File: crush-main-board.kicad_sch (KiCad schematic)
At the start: 37 parts, among them J1 4x4_Header, J10 3x3 Header, J11 3x3 Header, J12 3x2 Header, J13 3x4_Header, J14 3x4_Header, J15 2157601008, J16 Conn_01x02, J17 Conn_01x02, J2 4x4_Header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

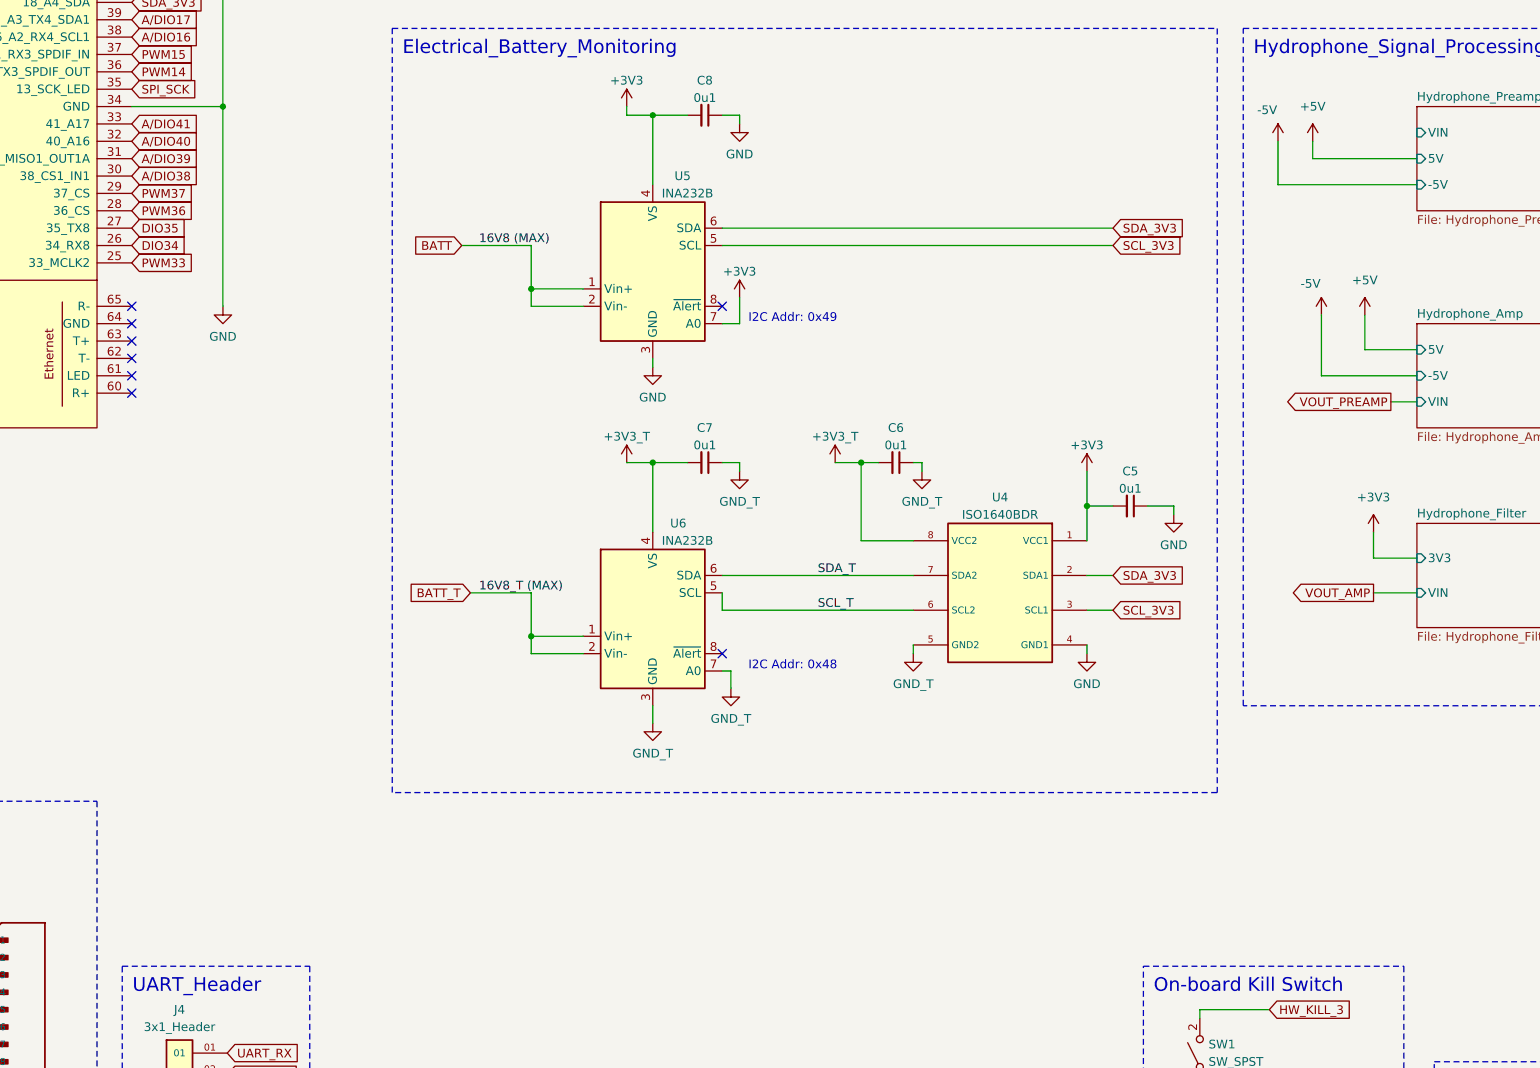
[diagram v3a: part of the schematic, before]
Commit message: Add BNC connection to VIN of hydrophone pre-amp subcircuit
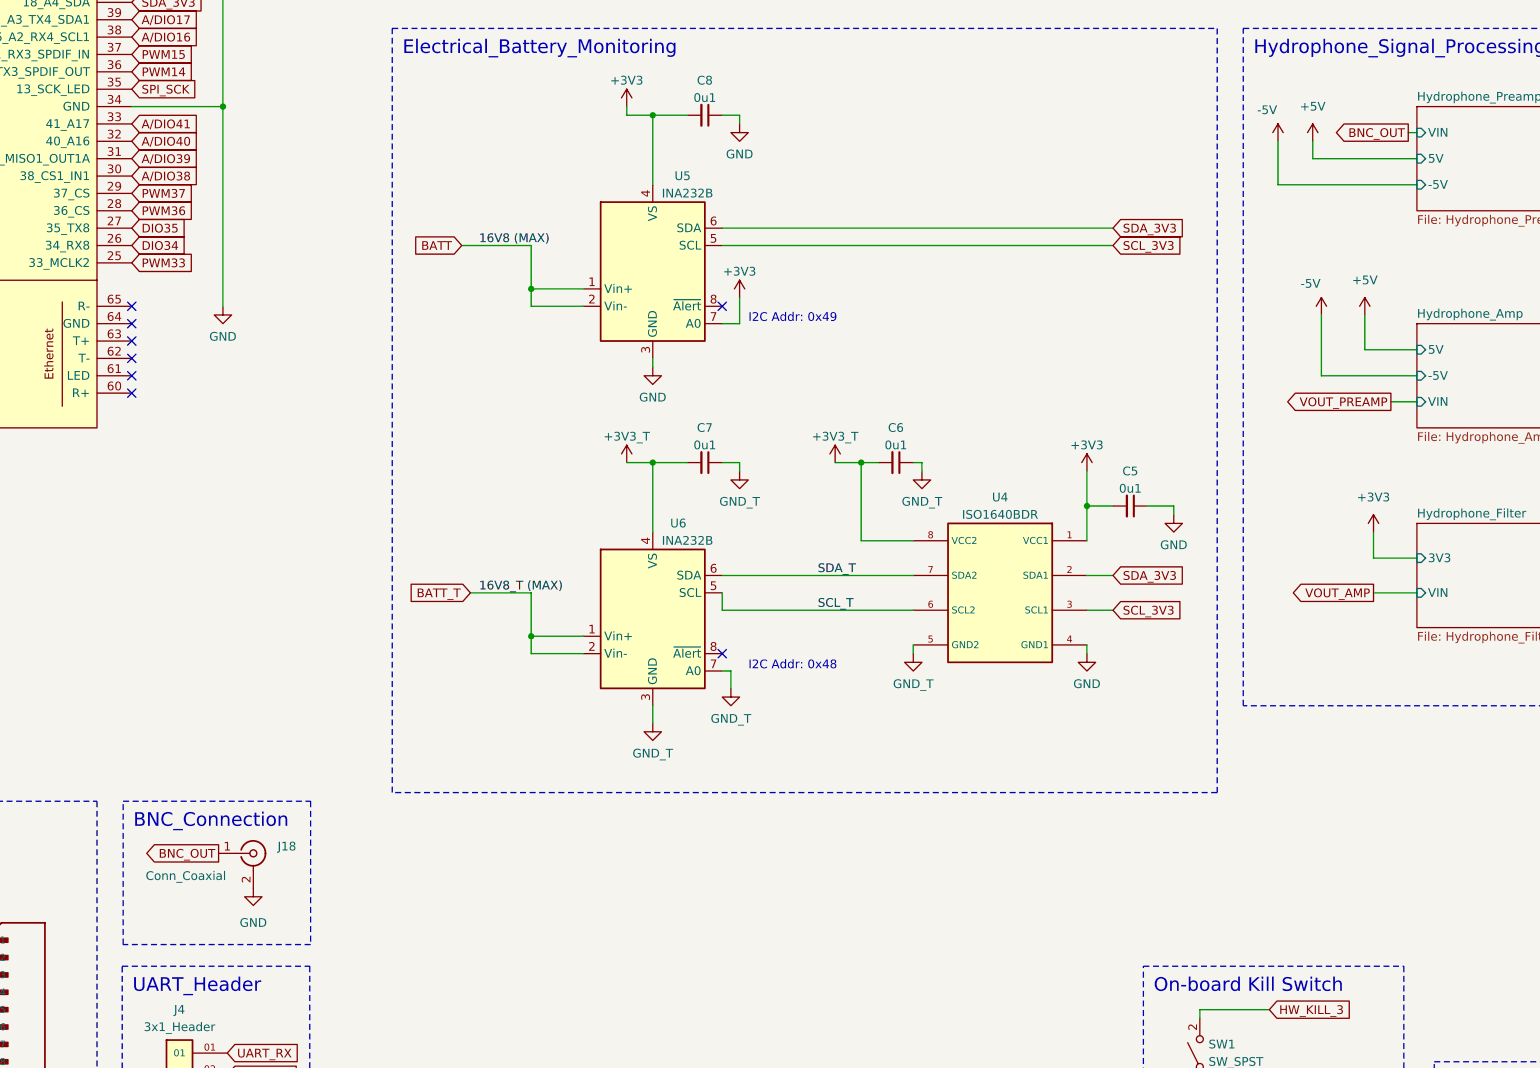
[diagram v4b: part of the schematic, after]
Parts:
- added J18: Conn_Coaxial, symbol Connector:Conn_Coaxial
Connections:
- net GND: now also J18.2 (Ext)
- new net BNC_OUT: J18.1 (In)
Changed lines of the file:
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@@
 		)
 	)
+	(text_box "BNC_Connection\n"
+		(exclude_from_sim no)
+		(at 77.47 156.21 0)
+		(size 27.432 20.955)
+		(margins 1.5 1.5 1.5 1.5)
+		(stroke
+			(width 0)
+			(type dash)
+		)
+		(fill
+			(type none)
+		)
+		(effects
+			(font
+				(size 2 2)
+			)
+			(justify left top)
+		)
+	)
 	(text_box "Thruster_PWM_to_ESC"
 		(exclude_from_sim no)
@@
 	(wire
 		(pts
+			(xy 265.43 58.42) (xy 266.7 58.42)
+		)
+		(stroke
+			(width 0)
+			(type default)
+		)
+	)
+	(wire
+		(pts
 			(xy 154.94 55.88) (xy 154.94 66.04)
 		)
@@
 		)
 	)
+	(global_label "BNC_OUT"
+		(shape output)
+		(at 265.43 58.42 180)
+		(fields_autoplaced yes)
+		(effects
+			(font
+				(size 1.27 1.27)
+			)
+			(justify right)
+		)
+		(property "Intersheetrefs" "${INTERSHEET_REFS}"
+			(at 253.9781 58.42 0)
+			(hide yes)
+			(show_name no)
+			(do_not_autoplace no)
+			(effects
+				(font
+					(size 1.27 1.27)
+				)
+				(justify right)
+			)
+		)
+	)
 	(global_label "SDA_3V3"
 		(shape input)
@@
 		)
 	)
+	(global_label "BNC_OUT"
+		(shape output)
+		(at 91.44 163.83 180)
+		(fields_autoplaced yes)
+		(effects
+			(font
+				(size 1.27 1.27)
+			)
+			(justify right)
+		)
+		(property "Intersheetrefs" "${INTERSHEET_REFS}"
+			(at 79.9881 163.83 0)
+			(hide yes)
+			(show_name no)
+			(do_not_autoplace no)
+			(effects
+				(font
+					(size 1.27 1.27)
+				)
+				(justify right)
+			)
+		)
+	)
 	(global_label "PWM15"
 		(shape input)
@@
 	)
 	(symbol
+		(lib_name "GND_1")
+		(lib_id "power:GND")
+		(at 96.52 168.91 0)
+		(unit 1)
+		(body_style 1)
+		(exclude_from_sim no)
+		(in_bom yes)
+		(on_board yes)
+		(in_pos_files yes)
+		(dnp no)
+		(fields_autoplaced yes)
+		(property "Reference" "#PWR083"
+			(at 96.52 175.26 0)
+			(hide yes)
+			(show_name no)
+			(do_not_autoplace no)
+			(effects
+				(font
+					(size 1.27 1.27)
+				)
+			)
+		)
+		(property "Value" "GND"
+			(at 96.52 173.99 0)
+			(show_name no)
+			(do_not_autoplace no)
+			(effects
+				(font
+					(size 1.27 1.27)
+				)
+			)
+		)
+		(property "Footprint" ""
+			(at 96.52 168.91 0)
+			(hide yes)
+			(show_name no)
+			(do_not_autoplace no)
+			(effects
+				(font
+					(size 1.27 1.27)
+				)
+			)
+		)
+		(property "Datasheet" ""
+			(at 96.52 168.91 0)
+			(hide yes)
+			(show_name no)
+			(do_not_autoplace no)
+			(effects
+				(font
+					(size 1.27 1.27)
+				)
+			)
+		)
+		(property "Description" "Power symbol creates a global label with name \"GND\" , ground"
+			(at 96.52 168.91 0)
+			(hide yes)
+			(show_name no)
+			(do_not_autoplace no)
+			(effects
+				(font
+					(size 1.27 1.27)
+				)
+			)
+		)
+		(pin "1"
+		)
+		(instances
+			(project "crush-main-board"
+				(path "/74b566fe-9d71-4817-95ed-d472d647f8c8"
+					(reference "#PWR083")
+					(unit 1)
+				)
+			)
+		)
+	)
+	(symbol
 		(lib_id "power:GND")
 		(at 24.13 240.03 0)
@@
 					(unit 1)
 				)
+			)
+		)
+	)
+	(symbol
+		(lib_id "Connector:Conn_Coaxial")
+		(at 96.52 163.83 0)
+		(unit 1)
+		(body_style 1)
+		(exclude_from_sim no)
+		(in_bom yes)
+		(on_board yes)
+		(in_pos_files yes)
+		(dnp no)
+		(property "Reference" "J18"
+			(at 100.076 162.814 0)
+			(show_name no)
+			(do_not_autoplace no)
+			(effects
+				(font
+					(size 1.27 1.27)
+				)
+				(justify left)
+			)
+		)
+		(property "Value" "Conn_Coaxial"
+			(at 80.772 167.132 0)
+			(show_name no)
+			(do_not_autoplace no)
+			(effects
+				(font
+					(size 1.27 1.27)
+				)
+				(justify left)
+			)
+		)
+		(property "Footprint" ""
+			(at 96.52 163.83 0)
+			(hide yes)
+			(show_name no)
+			(do_not_autoplace no)
+			(effects
+				(font
+					(size 1.27 1.27)
+				)
+			)
+		)
+		(property "Datasheet" ""
+			(at 96.52 163.83 0)
+			(hide yes)
+			(show_name no)
+			(do_not_autoplace no)
+			(effects
+				(font
+					(size 1.27 1.27)
+				)
+			)
+		)
+		(property "Description" "coaxial connector (BNC, SMA, SMB, SMC, Cinch/RCA, LEMO, ...)"
+			(at 96.52 163.83 0)
+			(hide yes)
+			(show_name no)
+			(do_not_autoplace no)
+			(effects
+				(font
+					(size 1.27 1.27)
+				)
+			)
+		)
+		(pin "2"
+		)
+		(pin "1"
+		)
+		(instances
+			(project "crush-main-board"
+				(path "/74b566fe-9d71-4817-95ed-d472d647f8c8"
+					(reference "J18")
+					(unit 1)
+				)

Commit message: Change op amps to single-supply LT6200
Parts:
- J18: footprint (none) -> Connector_Coaxial:BNC_Amphenol_031-5539_Vertical
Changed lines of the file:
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@@
 		(unit 1)
 		(body_style 1)
-		(exclude_from_sim no)
+		(exclude_from_sim yes)
 		(in_bom yes)
 		(on_board yes)
@@
 		(unit 1)
 		(body_style 1)
-		(exclude_from_sim yes)
+		(exclude_from_sim no)
 		(in_bom yes)
 		(on_board yes)
@@
 		(unit 1)
 		(body_style 1)
-		(exclude_from_sim no)
+		(exclude_from_sim yes)
 		(in_bom yes)
 		(on_board yes)
@@
 			)
 		)
-		(property "Footprint" ""
+		(property "Footprint" "Connector_Coaxial:BNC_Amphenol_031-5539_Vertical"
 			(at 96.52 163.83 0)
 			(hide yes)
@@
 		(unit 1)
 		(body_style 1)
-		(exclude_from_sim yes)
+		(exclude_from_sim no)
 		(in_bom yes)
 		(on_board yes)
@@
 		(unit 1)
 		(body_style 1)
-		(exclude_from_sim yes)
+		(exclude_from_sim no)
 		(in_bom yes)
 		(on_board yes)
@@
 		(unit 1)
 		(body_style 1)
-		(exclude_from_sim yes)
+		(exclude_from_sim no)
 		(in_bom yes)
 		(on_board yes)
@@
 		(unit 1)
 		(body_style 1)
-		(exclude_from_sim yes)
+		(exclude_from_sim no)
 		(in_bom yes)
 		(on_board yes)
@@
 		(unit 1)
 		(body_style 1)
-		(exclude_from_sim yes)
+		(exclude_from_sim no)
 		(in_bom yes)
 		(on_board yes)
@@
 		(unit 1)
 		(body_style 1)
-		(exclude_from_sim yes)
+		(exclude_from_sim no)
 		(in_bom yes)
 		(on_board yes)
@@
 		(unit 1)
 		(body_style 1)
-		(exclude_from_sim yes)
+		(exclude_from_sim no)
 		(in_bom yes)
 		(on_board yes)

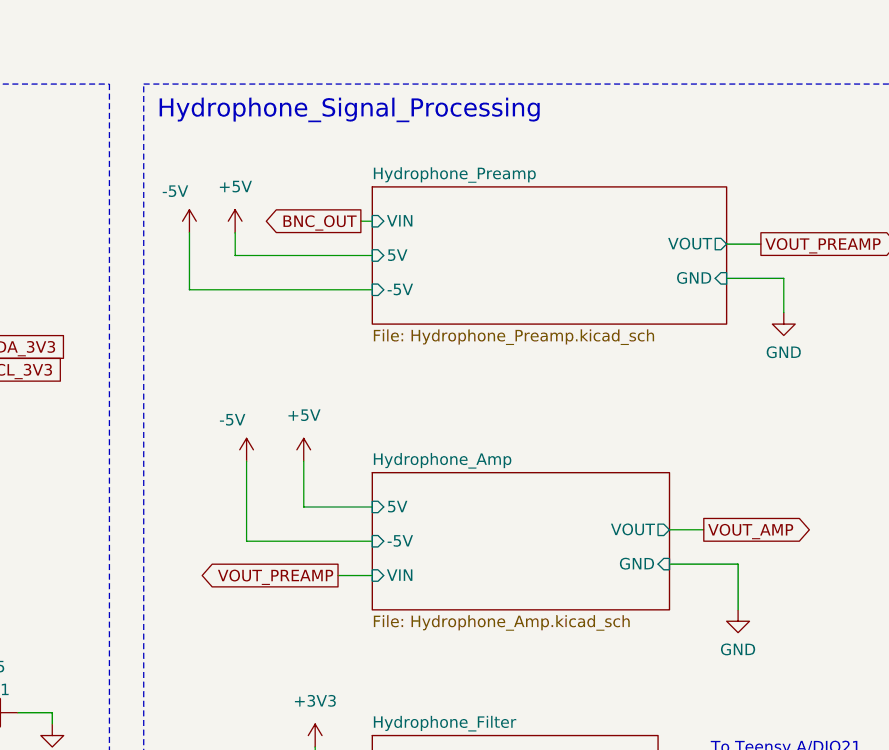
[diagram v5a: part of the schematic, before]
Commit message: Arranged all components off-board; considering swapping manual kill into empty space on bottom right corner to make room for hydrophone near A/DIO pins
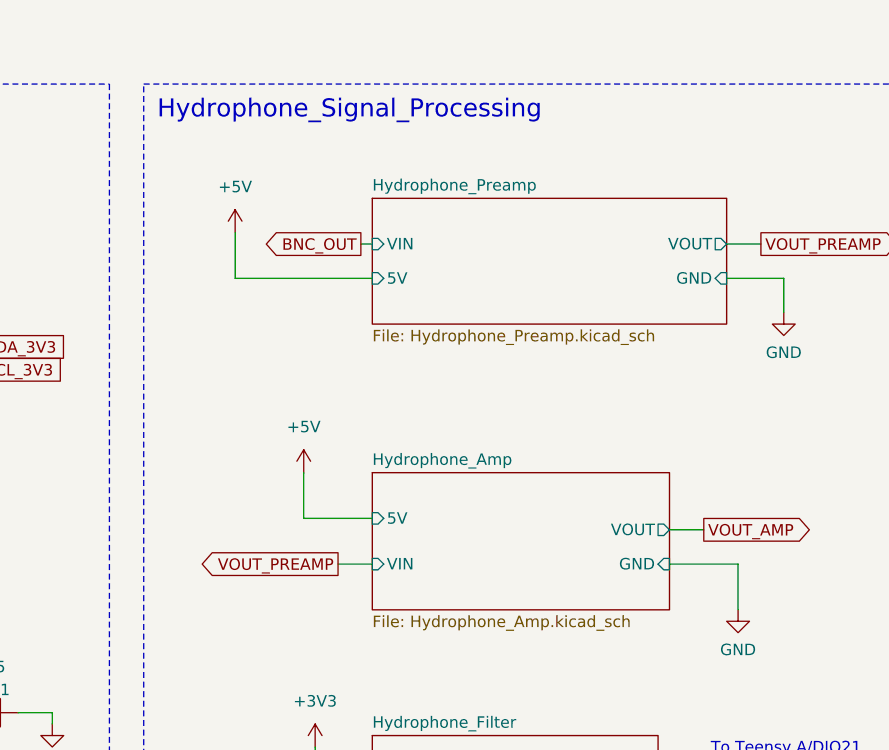
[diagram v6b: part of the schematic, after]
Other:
- sheet Hydrophone_Amp ports: added none; removed -5V
- sheet Hydrophone_Preamp ports: added none; removed -5V
